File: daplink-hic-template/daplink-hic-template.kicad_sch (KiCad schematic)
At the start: 1 part

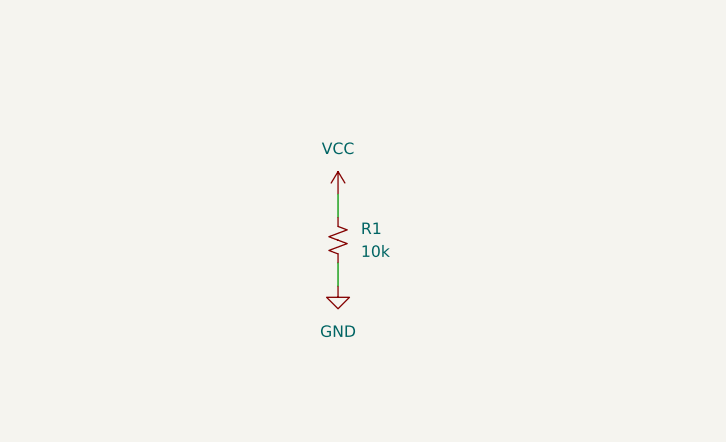
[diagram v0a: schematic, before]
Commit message: Added template files for the DAPLink HIC module
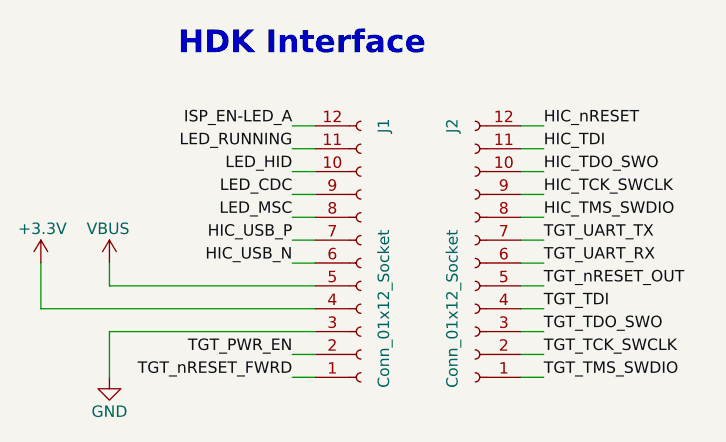
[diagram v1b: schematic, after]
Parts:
- removed R1: 10k, Resistor_SMD:R_0402_1005Metric, symbol Device:R_Small_US
- added J1, J2: Conn_01x12_Socket, Connector_PinHeader_2.54mm:PinHeader_1x12_P2.54mm_Vertical, symbol Connector:Conn_01x12_Socket
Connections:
- net GND: now also J1.3 (Pin_3)
- new net +3V3: J1.4 (Pin_4)
- new net HIC_TCK_SWCLK: J2.9 (Pin_9)
- new net HIC_TDI: J2.11 (Pin_11)
- new net HIC_TDO_SWO: J2.10 (Pin_10)
- new net HIC_TMS_SWDIO: J2.8 (Pin_8)
- new net HIC_USB_N: J1.6 (Pin_6)
- new net HIC_USB_P: J1.7 (Pin_7)
- new net HIC_nRESET: J2.12 (Pin_12)
- new net ISP_EN-LED_A: J1.12 (Pin_12)
- new net LED_CDC: J1.9 (Pin_9)
- new net LED_HID: J1.10 (Pin_10)
- new net LED_MSC: J1.8 (Pin_8)
- new net LED_RUNNING: J1.11 (Pin_11)
- new net TGT_PWR_EN: J1.2 (Pin_2)
- new net TGT_TCK_SWCLK: J2.2 (Pin_2)
- new net TGT_TDI: J2.4 (Pin_4)
- new net TGT_TDO_SWO: J2.3 (Pin_3)
- new net TGT_TMS_SWDIO: J2.1 (Pin_1)
- new net TGT_UART_RX: J2.6 (Pin_6)
- new net TGT_UART_TX: J2.7 (Pin_7)
- new net TGT_nRESET_FWRD: J1.1 (Pin_1)
- new net TGT_nRESET_OUT: J2.5 (Pin_5)
- new net VBUS: J1.5 (Pin_5)
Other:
- note added: "HDK Interface"
- title: PROJECT_TITLE_HERE -> DAPLink HIC Module - Template
